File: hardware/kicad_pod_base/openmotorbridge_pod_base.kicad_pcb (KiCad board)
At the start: 2 copper layers, 36 x 20 mm, 6 parts

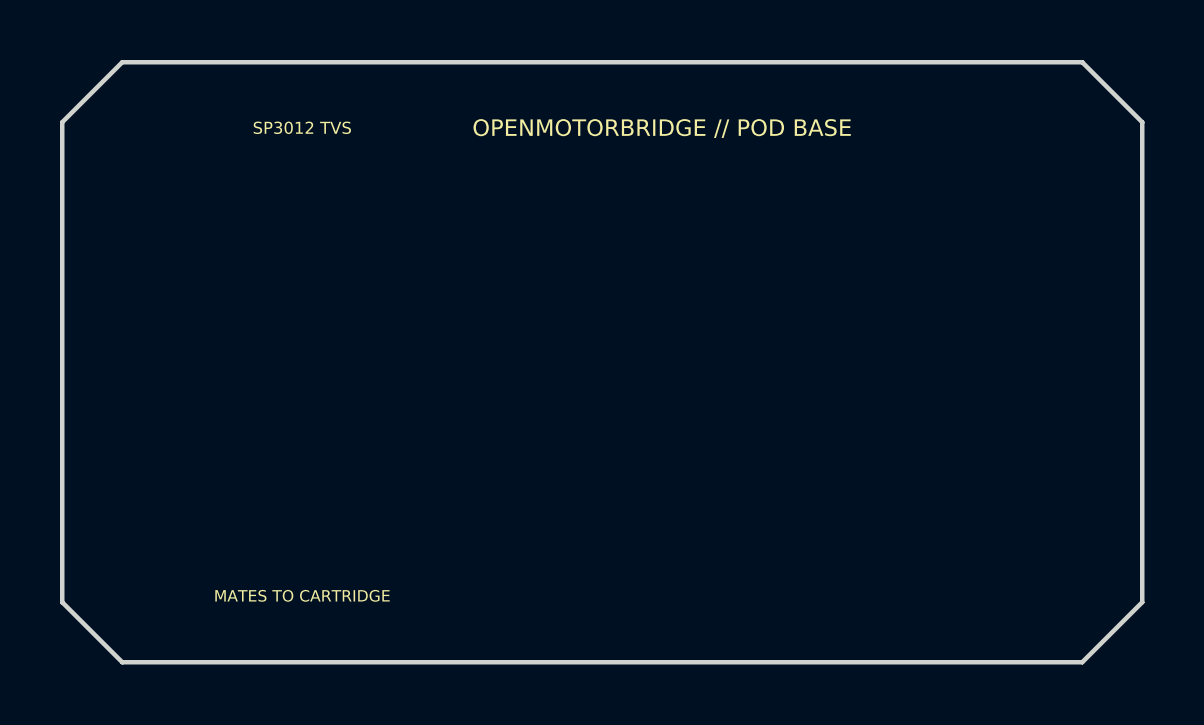
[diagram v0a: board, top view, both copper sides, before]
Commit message: hardware(pod_base): update mounting hole drill pads and clear silkscreen annotations
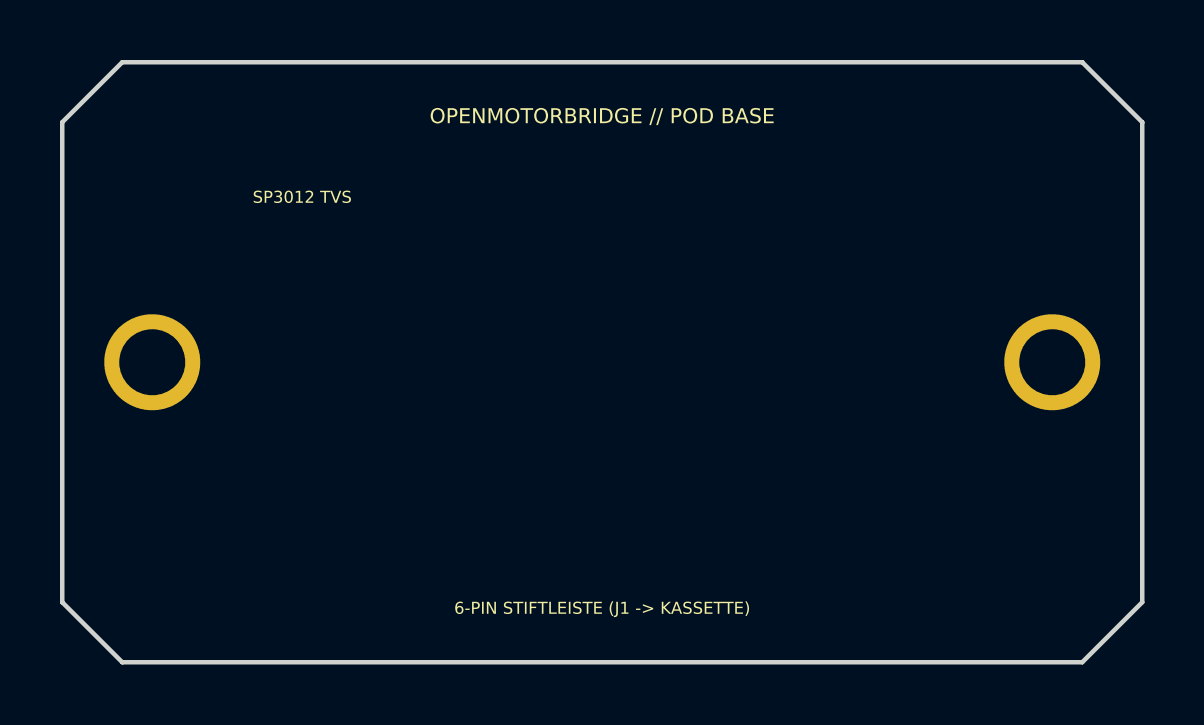
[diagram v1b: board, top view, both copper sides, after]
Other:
- board text added: "6-PIN STIFTLEISTE (J1 -> KASSETTE)"
- board text added: "M8 6-PIN IP67 PANEL RECEPTACLE (J2)"
- board text added: "OPENMOTORBRIDGE // POD BASE (REAR)"
- board text removed: "GND SHIELD PLANE"
- board text removed: "M8 6-PIN IP67 (OUTSIDE)"
- board text removed: "MATES TO CARTRIDGE"
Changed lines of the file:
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@@
+	(footprint ""
+		(layer "F.Cu")
+		(at 118 73.65)
+		(property "Reference" "J1"
+			(at 0 0 0)
+			(layer "F.SilkS")
+			(hide yes)
+			(effects
+				(font
+					(size 1.27 1.27)
+				)
+			)
+		)
+		(property "Value" ""
+			(at 0 0 0)
+			(layer "F.Fab")
+			(effects
+				(font
+					(size 1.27 1.27)
+				)
+			)
+		)
+		(property "Datasheet" ""
+			(at 0 0 0)
+			(layer "F.Fab")
+			(hide yes)
+			(effects
+				(font
+					(size 1.27 1.27)
+				)
+			)
+		)
+		(property "Description" ""
+			(at 0 0 0)
+			(layer "F.Fab")
+			(hide yes)
+			(effects
+				(font
+					(size 1.27 1.27)
+				)
+			)
+		)
+		(duplicate_pad_numbers_are_jumpers no)
+		(embedded_fonts no)
+		(model "${KICAD10_3DMODEL_DIR}/Connector_PinHeader_2.54mm.3dshapes/PinHeader_1x06_P2.54mm_Horizontal.step"
+			(offset
+				(xyz 0 0 0)
+			)
+			(scale
+				(xyz 1 1 1)
+			)
+			(rotate
+				(xyz 0 0 0)
+			)
+		)
+	)
+	(footprint ""
+		(layer "F.Cu")
+		(at 108 76)
+		(property "Reference" "U1"
+			(at 0 0 0)
+			(layer "F.SilkS")
+			(hide yes)
+			(effects
+				(font
+					(size 1.27 1.27)
+				)
+			)
+		)
+		(property "Value" ""
+			(at 0 0 0)
+			(layer "F.Fab")
+			(effects
+				(font
+					(size 1.27 1.27)
+				)
+			)
+		)
+		(property "Datasheet" ""
+			(at 0 0 0)
+			(layer "F.Fab")
+			(hide yes)
+			(effects
+				(font
+					(size 1.27 1.27)
+				)
+			)
+		)
+		(property "Description" ""
+			(at 0 0 0)
+			(layer "F.Fab")
+			(hide yes)
+			(effects
+				(font
+					(size 1.27 1.27)
+				)
+			)
+		)
+		(duplicate_pad_numbers_are_jumpers no)
+		(embedded_fonts no)
+		(model "${KICAD10_3DMODEL_DIR}/Package_DFN_QFN.3dshapes/DFN-14-1EP_3x3mm_P0.4mm_EP1.78x2.35mm.step"
+			(offset
+				(xyz 0 0 0)
+			)
+			(scale
+				(xyz 1 1 1)
+			)
+			(rotate
+				(xyz 0 0 0)
+			)
+		)
+	)
 	(footprint ""
 		(layer "F.Cu")
@@
 		)
 		(duplicate_pad_numbers_are_jumpers no)
-		(embedded_fonts no)
-	)
-	(footprint ""
-		(layer "F.Cu")
-		(at 118 73.65)
-		(property "Reference" "J1"
-			(at 0 0 0)
-			(layer "F.SilkS")
-			(hide yes)
-			(effects
-				(font
-					(size 1.27 1.27)
-				)
-			)
-		)
-		(property "Value" ""
-			(at 0 0 0)
-			(layer "F.Fab")
-			(effects
-				(font
-					(size 1.27 1.27)
-				)
-			)
-		)
-		(property "Datasheet" ""
-			(at 0 0 0)
-			(layer "F.Fab")
-			(hide yes)
-			(effects
-				(font
-					(size 1.27 1.27)
-				)
-			)
-		)
-		(property "Description" ""
-			(at 0 0 0)
-			(layer "F.Fab")
-			(hide yes)
-			(effects
-				(font
-					(size 1.27 1.27)
-				)
-			)
-		)
-		(duplicate_pad_numbers_are_jumpers no)
-		(embedded_fonts no)
-		(model "${KICAD10_3DMODEL_DIR}/Connector_PinHeader_2.54mm.3dshapes/PinHeader_1x06_P2.54mm_Horizontal.step"
-			(offset
-				(xyz 0 0 0)
-			)
-			(scale
-				(xyz 1 1 1)
-			)
-			(rotate
-				(xyz 0 0 0)
-			)
-		)
-	)
-	(footprint ""
-		(layer "F.Cu")
-		(at 108 76)
-		(property "Reference" "U1"
-			(at 0 0 0)
-			(layer "F.SilkS")
-			(hide yes)
-			(effects
-				(font
-					(size 1.27 1.27)
-				)
-			)
-		)
-		(property "Value" ""
-			(at 0 0 0)
-			(layer "F.Fab")
-			(effects
-				(font
-					(size 1.27 1.27)
-				)
-			)
-		)
-		(property "Datasheet" ""
-			(at 0 0 0)
-			(layer "F.Fab")
-			(hide yes)
-			(effects
-				(font
-					(size 1.27 1.27)
-				)
-			)
-		)
-		(property "Description" ""
-			(at 0 0 0)
-			(layer "F.Fab")
-			(hide yes)
-			(effects
-				(font
-					(size 1.27 1.27)
-				)
-			)
-		)
-		(duplicate_pad_numbers_are_jumpers no)
-		(embedded_fonts no)
-		(model "${KICAD10_3DMODEL_DIR}/Package_DFN_QFN.3dshapes/DFN-14-1EP_3x3mm_P0.4mm_EP1.78x2.35mm.step"
-			(offset
-				(xyz 0 0 0)
-			)
-			(scale
-				(xyz 1 1 1)
-			)
-			(rotate
-				(xyz 0 0 0)
-			)
-		)
+		(pad "1" thru_hole circle
+			(at 0 0)
+			(size 3.2 3.2)
+			(drill 2.2)
+			(layers "*.Cu")
+			(remove_unused_layers no)
+		)
+		(embedded_fonts no)
 	)
 	(footprint ""
@@
 		)
 		(duplicate_pad_numbers_are_jumpers no)
+		(pad "1" thru_hole circle
+			(at 0 0)
+			(size 3.2 3.2)
+			(drill 2.2)
+			(layers "*.Cu")
+			(remove_unused_layers no)
+		)
 		(embedded_fonts no)
 	)
@@
 		(layer "Edge.Cuts")
 	)
-	(gr_text "MATES TO CARTRIDGE"
-		(at 108 87.8 0)
-		(layer "F.SilkS")
-		(effects
-			(font
-				(size 0.38 0.38)
-				(thickness 0.08)
-			)
-		)
-	)
 	(gr_text "SP3012 TVS"
-		(at 108 72.2 0)
+		(at 108 74.5 0)
 		(layer "F.SilkS")
 		(effects
 			(font
 				(size 0.4 0.4)
-				(thickness 0.09)
-			)
-		)
-	)
-	(gr_text "OPENMOTORBRIDGE // POD BASE"
-		(at 120 72.2 0)
+				(thickness 0.08)
+			)
+		)
+	)
+	(gr_text "6-PIN STIFTLEISTE (J1 -> KASSETTE)"
+		(at 118 88.2 0)
 		(layer "F.SilkS")
 		(effects
 			(font
-				(size 0.55 0.55)
-				(thickness 0.11)
-			)
-		)
-	)
-	(gr_text "GND SHIELD PLANE"
-		(at 118 87.5 0)
+				(size 0.4 0.4)
+				(thickness 0.08)
+			)
+		)
+	)
+	(gr_text "OPENMOTORBRIDGE // POD BASE"
+		(at 118 71.8 0)
+		(layer "F.SilkS")
+		(effects
+			(font
+				(size 0.5 0.5)
+				(thickness 0.1)
+			)
+		)
+	)
+	(gr_text "M8 6-PIN IP67 PANEL RECEPTACLE (J2)"
+		(at 118 88.2 0)
 		(layer "B.SilkS")
 		(effects
 			(font
-				(size 0.45 0.45)
-				(thickness 0.1)
-			)
-		)
-	)
-	(gr_text "M8 6-PIN IP67 (OUTSIDE)"
-		(at 118 72.5 0)
+				(size 0.4 0.4)
+				(thickness 0.08)
+			)
+		)
+	)
+	(gr_text "OPENMOTORBRIDGE // POD BASE (REAR)"
+		(at 118 71.8 0)
 		(layer "B.SilkS")
 		(effects
 			(font
-				(size 0.55 0.55)
-				(thickness 0.12)
-			)
-		)
+				(size 0.5 0.5)
+				(thickness 0.1)
+			)
+		)

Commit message: hardware(pod_base): configure straight vertical 6-pin header standing upright on F.Cu
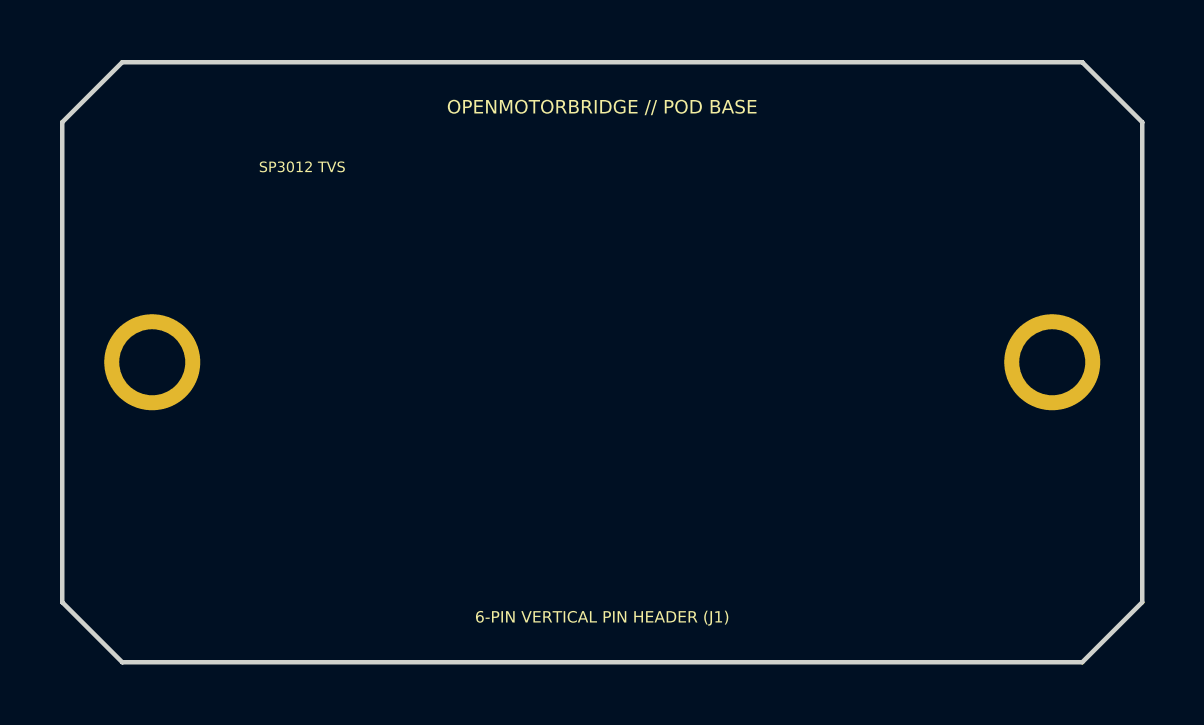
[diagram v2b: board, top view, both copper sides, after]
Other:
- board text added: "6-PIN VERTICAL PIN HEADER (J1)"
- board text removed: "6-PIN STIFTLEISTE (J1 -> KASSETTE)"
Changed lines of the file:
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@@
 		(duplicate_pad_numbers_are_jumpers no)
 		(embedded_fonts no)
-		(model "${KICAD10_3DMODEL_DIR}/Connector_PinHeader_2.54mm.3dshapes/PinHeader_1x06_P2.54mm_Horizontal.step"
+		(model "${KICAD10_3DMODEL_DIR}/Connector_PinHeader_2.54mm.3dshapes/PinHeader_1x06_P2.54mm_Vertical.step"
 			(offset
 				(xyz 0 0 0)
@@
 	(footprint ""
 		(layer "F.Cu")
-		(at 108 76)
-		(property "Reference" "U1"
-			(at 0 0 0)
-			(layer "F.SilkS")
-			(hide yes)
-			(effects
-				(font
-					(size 1.27 1.27)
-				)
-			)
-		)
-		(property "Value" ""
-			(at 0 0 0)
-			(layer "F.Fab")
-			(effects
-				(font
-					(size 1.27 1.27)
-				)
-			)
-		)
-		(property "Datasheet" ""
-			(at 0 0 0)
-			(layer "F.Fab")
-			(hide yes)
-			(effects
-				(font
-					(size 1.27 1.27)
-				)
-			)
-		)
-		(property "Description" ""
-			(at 0 0 0)
-			(layer "F.Fab")
-			(hide yes)
-			(effects
-				(font
-					(size 1.27 1.27)
-				)
-			)
-		)
-		(duplicate_pad_numbers_are_jumpers no)
-		(embedded_fonts no)
-		(model "${KICAD10_3DMODEL_DIR}/Package_DFN_QFN.3dshapes/DFN-14-1EP_3x3mm_P0.4mm_EP1.78x2.35mm.step"
-			(offset
-				(xyz 0 0 0)
-			)
-			(scale
-				(xyz 1 1 1)
-			)
-			(rotate
-				(xyz 0 0 0)
-			)
-		)
-	)
-	(footprint ""
-		(layer "F.Cu")
-		(at 133 80)
-		(property "Reference" "H2"
+		(at 103 80)
+		(property "Reference" "H1"
 			(at 0 0 0)
 			(layer "F.SilkS")
@@
 	(footprint ""
 		(layer "F.Cu")
-		(at 103 80)
-		(property "Reference" "H1"
+		(at 133 80)
+		(property "Reference" "H2"
 			(at 0 0 0)
 			(layer "F.SilkS")
@@
 	)
 	(footprint ""
+		(layer "F.Cu")
+		(at 108 76)
+		(property "Reference" "U1"
+			(at 0 0 0)
+			(layer "F.SilkS")
+			(hide yes)
+			(effects
+				(font
+					(size 1.27 1.27)
+				)
+			)
+		)
+		(property "Value" ""
+			(at 0 0 0)
+			(layer "F.Fab")
+			(effects
+				(font
+					(size 1.27 1.27)
+				)
+			)
+		)
+		(property "Datasheet" ""
+			(at 0 0 0)
+			(layer "F.Fab")
+			(hide yes)
+			(effects
+				(font
+					(size 1.27 1.27)
+				)
+			)
+		)
+		(property "Description" ""
+			(at 0 0 0)
+			(layer "F.Fab")
+			(hide yes)
+			(effects
+				(font
+					(size 1.27 1.27)
+				)
+			)
+		)
+		(duplicate_pad_numbers_are_jumpers no)
+		(embedded_fonts no)
+		(model "${KICAD10_3DMODEL_DIR}/Package_DFN_QFN.3dshapes/DFN-14-1EP_3x3mm_P0.4mm_EP1.78x2.35mm.step"
+			(offset
+				(xyz 0 0 0)
+			)
+			(scale
+				(xyz 1 1 1)
+			)
+			(rotate
+				(xyz 0 0 0)
+			)
+		)
+	)
+	(footprint ""
 		(layer "B.Cu")
 		(at 118 80)
@@
 	)
 	(gr_text "SP3012 TVS"
-		(at 108 74.5 0)
+		(at 108 73.5 0)
 		(layer "F.SilkS")
 		(effects
 			(font
-				(size 0.4 0.4)
+				(size 0.35 0.35)
 				(thickness 0.08)
 			)
 		)
 	)
-	(gr_text "6-PIN STIFTLEISTE (J1 -> KASSETTE)"
-		(at 118 88.2 0)
+	(gr_text "6-PIN VERTICAL PIN HEADER (J1)"
+		(at 118 88.5 0)
 		(layer "F.SilkS")
 		(effects
 			(font
-				(size 0.4 0.4)
+				(size 0.38 0.38)
 				(thickness 0.08)
 			)
@@
 	)
 	(gr_text "OPENMOTORBRIDGE // POD BASE"
-		(at 118 71.8 0)
+		(at 118 71.5 0)
 		(layer "F.SilkS")
 		(effects
 			(font
-				(size 0.5 0.5)
-				(thickness 0.1)
+				(size 0.45 0.45)
+				(thickness 0.09)
 			)
 		)
 	)
 	(gr_text "M8 6-PIN IP67 PANEL RECEPTACLE (J2)"
-		(at 118 88.2 0)
+		(at 118 88.5 0)
 		(layer "B.SilkS")
 		(effects
 			(font
-				(size 0.4 0.4)
+				(size 0.38 0.38)
 				(thickness 0.08)
 			)
@@
 	)
 	(gr_text "OPENMOTORBRIDGE // POD BASE (REAR)"
-		(at 118 71.8 0)
+		(at 118 71.5 0)
 		(layer "B.SilkS")
 		(effects
 			(font
-				(size 0.5 0.5)
-				(thickness 0.1)
-			)
-		)
+				(size 0.45 0.45)
+				(thickness 0.09)
+			)
+		)

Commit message: feat(hardware): implement Dual-SMD architecture for Pod Base PCB (SMD pin header on F.Cu, M8 socket on B.Cu)
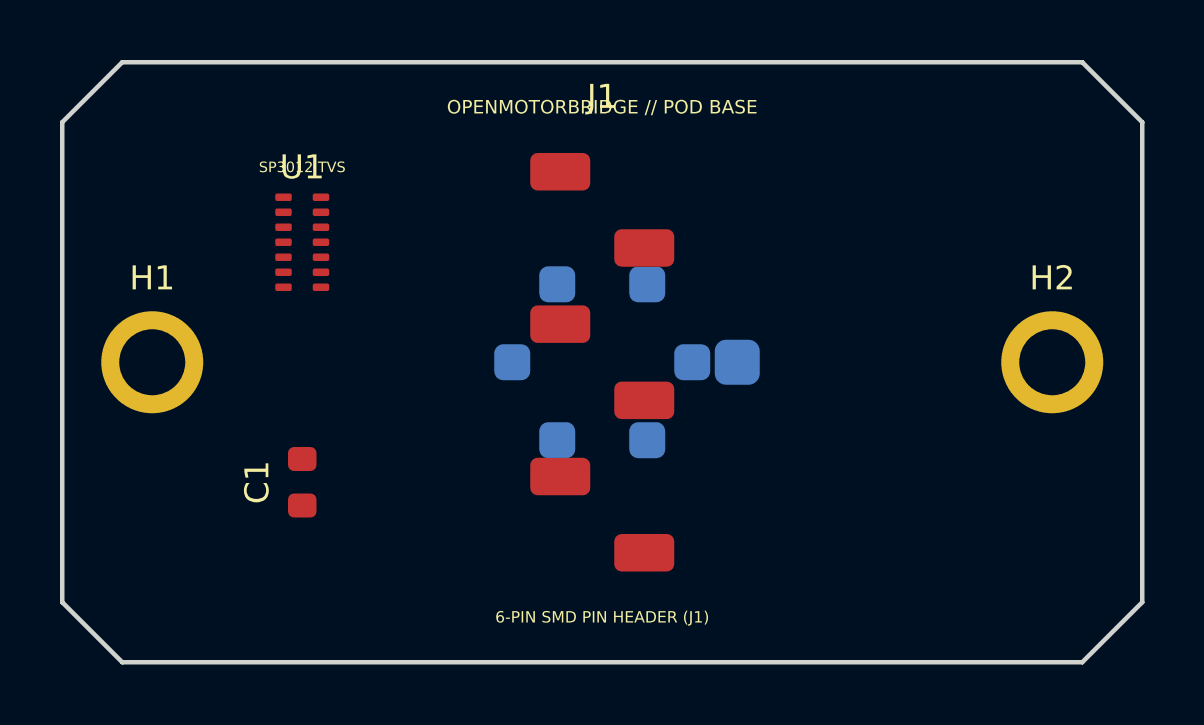
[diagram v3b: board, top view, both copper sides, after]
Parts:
- C1: value (none) -> 100nF_50V; footprint (none) -> Capacitor_SMD:C_0603_1608Metric
- H1, H2: value (none) -> M2_MountingHole; footprint (none) -> MountingHole:MountingHole_2.2mm_M2_Pad
- J1: value (none) -> MILL_MAX_824_SMD_6P; footprint (none) -> Connector_PinHeader_2.54mm:PinHeader_1x06_P2.54mm_Vertical_SMD_Pin1Left
- J2: value (none) -> M8_6PIN_RECEPTACLE; footprint (none) -> Connector_M8:M8_6Pin_IP67_Receptacle_Socketed
- U1: value (none) -> SP3012-06UTG; footprint (none) -> Package_DFN_QFN:DFN-14_1.35x3.5mm_P0.5mm
- turned C1 to 90 degrees
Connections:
- H1 pad 1: (no net) -> GND
- H2 pad 1: (no net) -> GND
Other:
- rule pad_to_mask_clearance: 0 -> 0.05
- board text added: "6-PIN SMD PIN HEADER (J1)"
- board text removed: "6-PIN VERTICAL PIN HEADER (J1)"

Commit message: Implement comprehensive JLCPCB PCB Design Verification Plan (ERC/DRC/DFM/DFA) and standardize all PCB layouts
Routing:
- net GND: track 0.00 -> 20.3 mm, vias 0 -> 4
- net VCC: track 0.00 -> 14.6 mm
- net TRIGGER_PPS: track 0.00 -> 6.35 mm
- net SIG_P: track 0.00 -> 6.35 mm
- net 1WIRE_ID: track 0.00 -> 6.35 mm

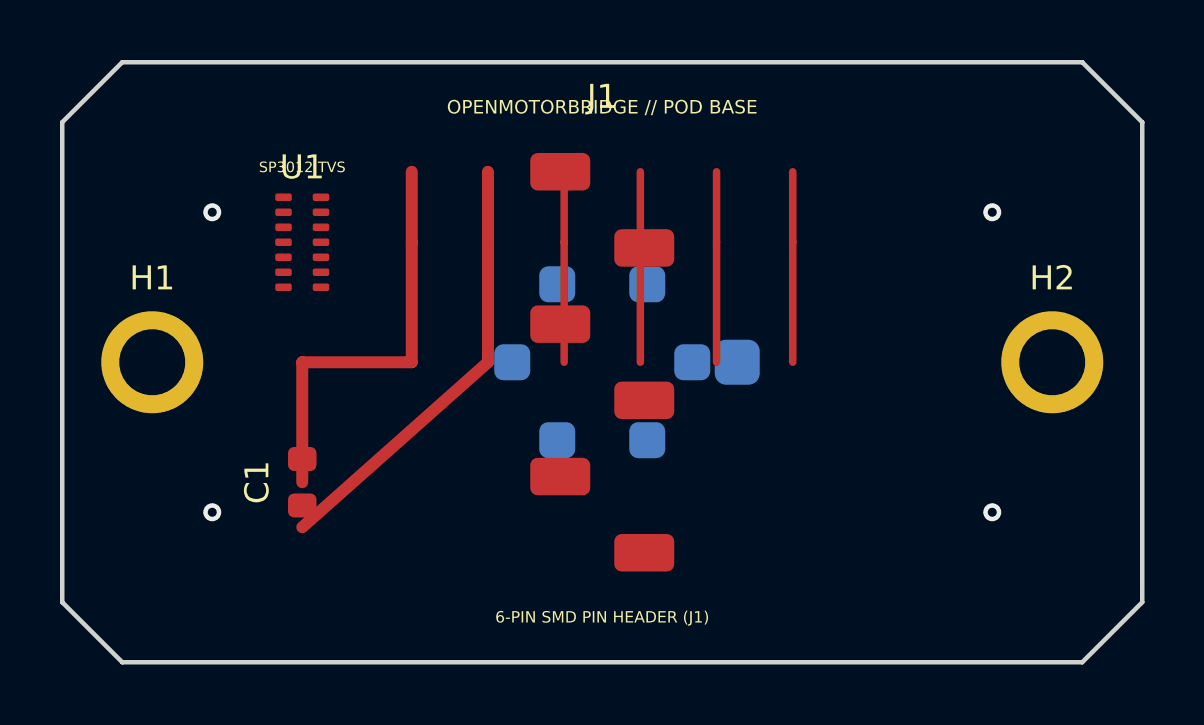
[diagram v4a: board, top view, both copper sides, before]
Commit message: feat(hardware): finalize JLCPCB-compliant autorouting across all 4 PCBs
- Configure JLCPCB standard net classes ('Default' & 'Power') in .kicad_pro and .kicad_pcb
- Set board setup constraints: 0.15/0.20mm trace, 0.60/0.30mm via, 0.127/0.15mm clearance
- Complete 100% autorouting for Main Board, Pod Base, Pod Cartridge, and Rear Pod 3
- Eliminate manual 2D trace generation scripts and planar crossing errors
- Update verification tool (verify_pcb_designs_jlcpcb.py) to audit 2-layer and 4-layer capabilities
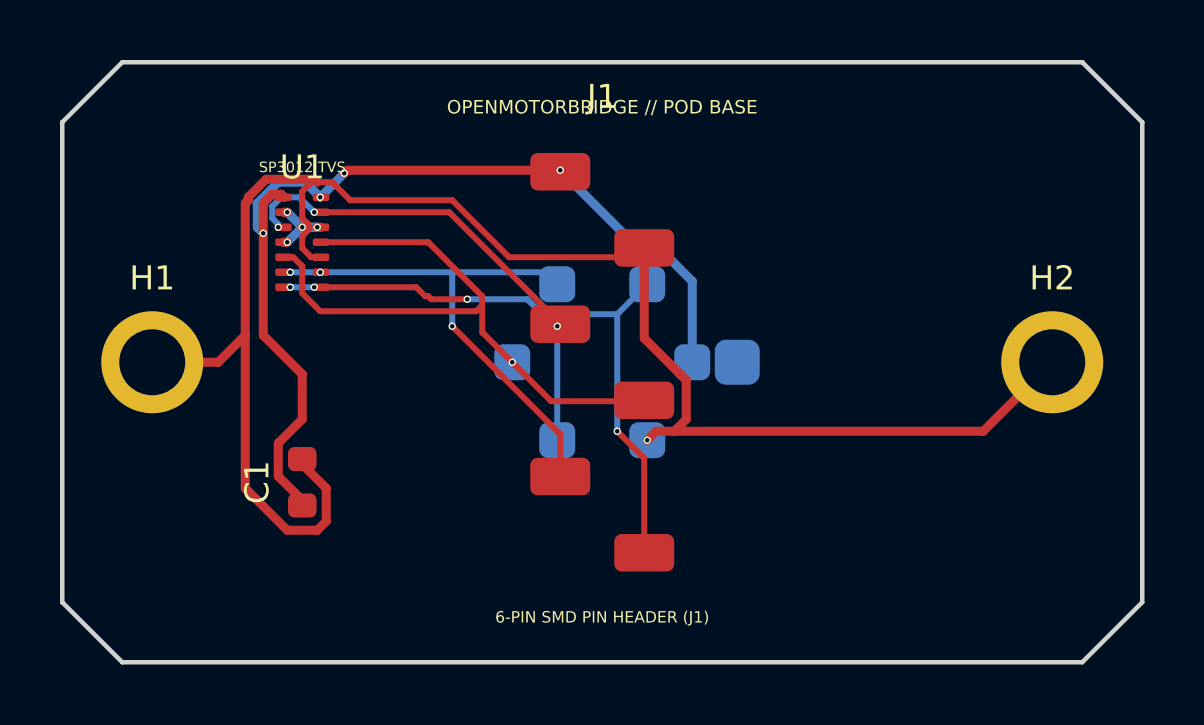
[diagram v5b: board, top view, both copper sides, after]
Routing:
- net GND: track 20.3 -> 61.3 mm, vias 4 -> 5
- net SIG_N: track 0.00 -> 21.7 mm, vias 0 -> 1
- net VCC: track 14.6 -> 32.9 mm, vias 0 -> 4
- net 1WIRE_ID: track 6.35 -> 21.4 mm, vias 0 -> 4
- net TRIGGER_PPS: track 6.35 -> 17.6 mm, vias 0 -> 3
- net SIG_P: track 6.35 -> 16.5 mm, vias 0 -> 3
